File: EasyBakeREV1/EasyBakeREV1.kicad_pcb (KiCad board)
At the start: 2 copper layers, 100 x 71.2 mm, 135 parts, among them Q1 MMBT2222A, Q2 MMBT2222A, Q3 MMBT2222A, Q4 MMBT2222A, U1 MIC5219-3.3YM5, U10 STP08CP05, U11 MIC5219-5.0YM5, U12 NLSV2T244MU, U2 USBLC6-2SC6, U3 PCA9702, U4 SQ2310ES_SOT23, U5 NHD-C12832A1Z, U6 SQ2310ES_SOT23, U7 MAX31855_SO8, U8 LM324, U9 SN74LVC1G32, Y1 12MHz

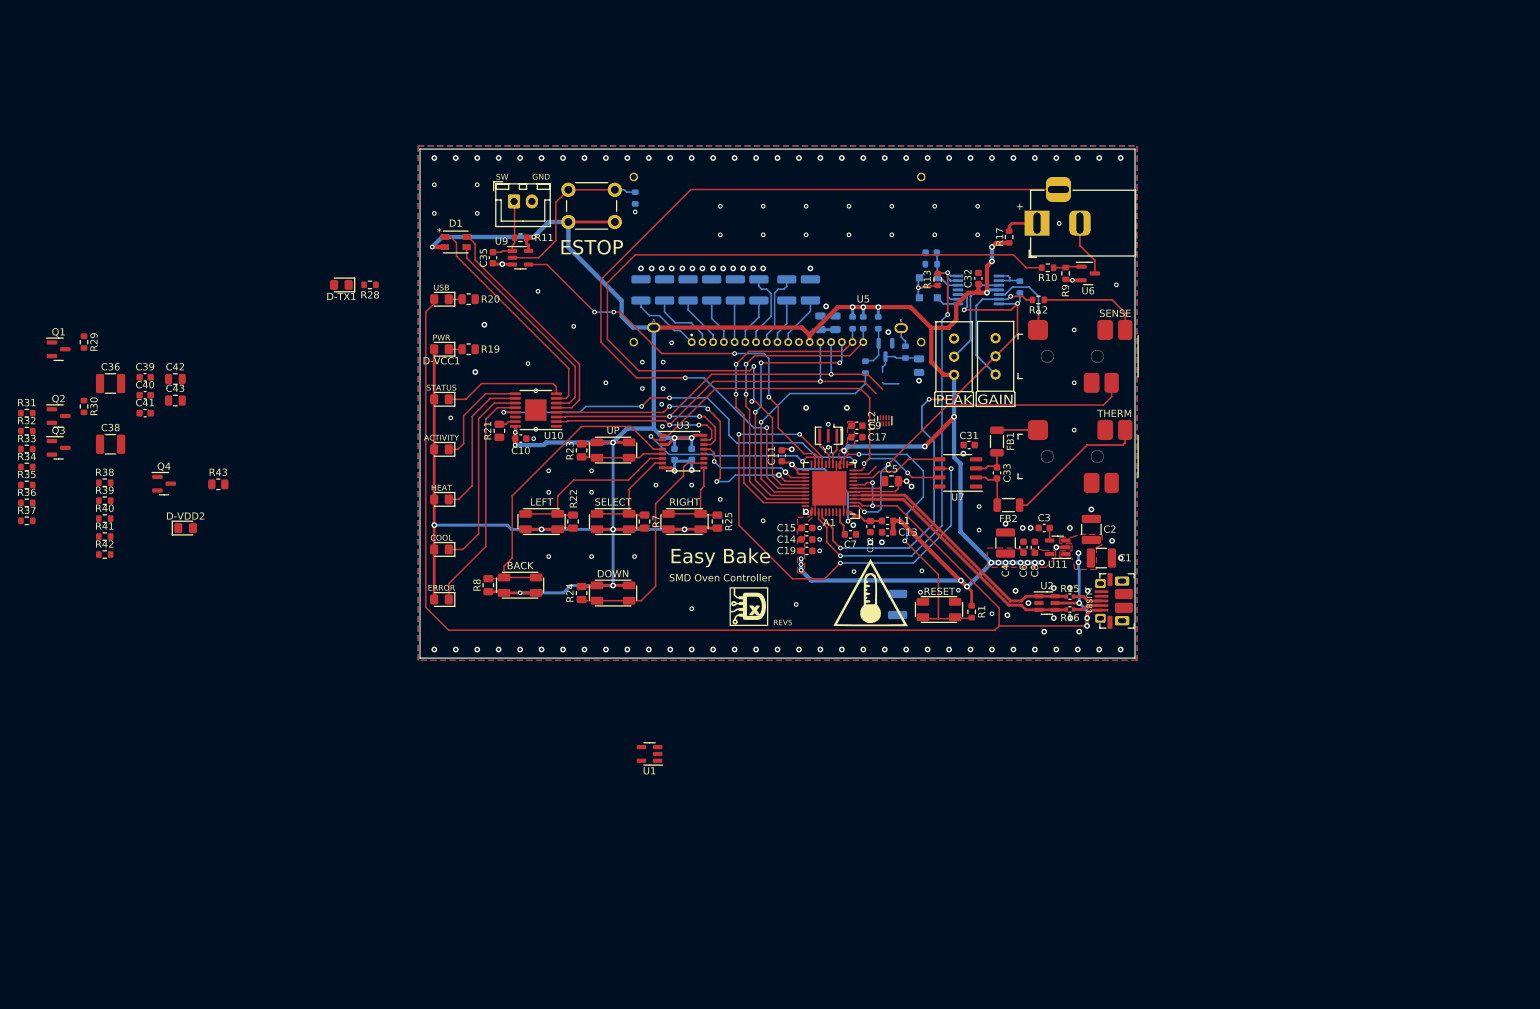
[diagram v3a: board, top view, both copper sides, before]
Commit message: Replaced MCU - started layout
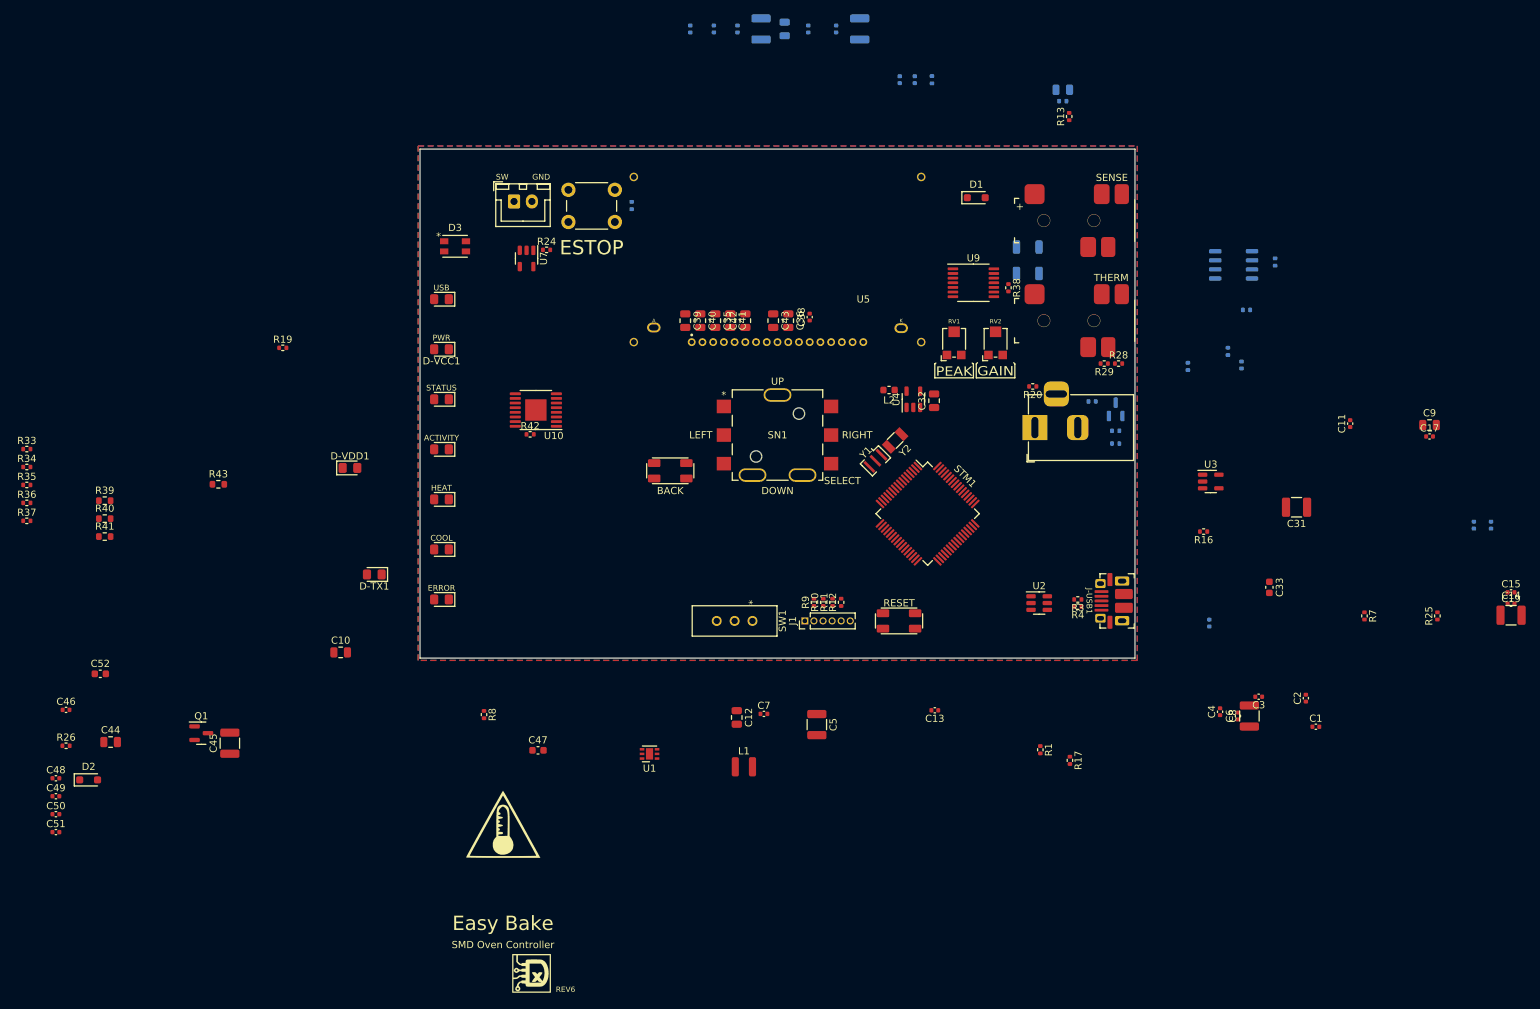
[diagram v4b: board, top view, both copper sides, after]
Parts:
- removed A1: PRO-MICRO-IC, Daxxn_Packages:QFN-44-1EP_7x7mm_P0.5mm_EP4.8x4.8mm
- removed D-VDD2: YELLOW, LED_SMD:LED_0805_2012Metric_Pad1.15x1.40mm_HandSolder
- removed D5, D6: General, Diode_SMD:D_SOD-323_HandSoldering
- removed Q2, Q3, Q4: MMBT2222A, Package_TO_SOT_SMD:SOT-23
- removed R30, R31: 10K, Resistor_SMD:R_0603_1608Metric
- removed R32: 1K, Resistor_SMD:R_0603_1608Metric
- removed SW-M-DN1, SW-M-L1, SW-M-R1, SW-M-UP1: SW_SPST, Daxxn_Switches:TL3365AF180QG
- removed SW-M-SEL1: TL3365, Daxxn_Switches:TL3365AF180QG
- removed U11: MIC5219-5.0YM5, Package_TO_SOT_SMD:SOT-23-5
- removed U12: NLSV2T244MU, Package_DFN_QFN:OnSemi_UDFN-8_1.2x1.8mm_P0.4mm
- added C44: 1uF, Capacitor_SMD:C_0805_2012Metric, F.Cu at (-28.3, 102.9)
- added C45: 10uF, Capacitor_SMD:C_1210_3225Metric, F.Cu at (-11.6, 103.1)
- added C46: 100nF, Capacitor_SMD:C_0402_1005Metric, F.Cu at (-34.5, 98.4)
- added C47: 100nF, Capacitor_SMD:C_0603_1608Metric, F.Cu at (31.5, 104.1)
- added C48: 100nF, Capacitor_SMD:C_0402_1005Metric, F.Cu at (-35.9, 108.0)
- added C49: 10nF, Capacitor_SMD:C_0402_1005Metric, F.Cu at (-35.9, 110.5)
- added C50: 100nF, Capacitor_SMD:C_0402_1005Metric, F.Cu at (-35.9, 113.0)
- added C51: 100nF, Capacitor_SMD:C_0402_1005Metric, F.Cu at (-35.9, 115.5)
- added C52: 100nF, Capacitor_SMD:C_0603_1608Metric, F.Cu at (-29.7, 93.4)
- added D-VDD1: YELLOW, LED_SMD:LED_0805_2012Metric_Pad1.15x1.40mm_HandSolder, F.Cu at (5.20, 64.6)
- added D2: General, Diode_SMD:D_SOD-323_HandSoldering, F.Cu at (-31.4, 108.2)
- added D3: LED_RGBA, Daxxn_LEDs:IN-P32TATRGB, F.Cu at (19.9, 33.6)
- added J1: SWD, Connector_PinHeader_1.27mm:PinHeader_1x06_P1.27mm_Vertical, F.Cu at (68.8, 86.0)
- added L2: 100nH, Inductor_SMD:L_0603_1608Metric, F.Cu at (80.6, 53.7)
- added R26: 22, Resistor_SMD:R_0402_1005Metric, F.Cu at (-34.5, 103.5)
- added SN1: JS5208, Daxxn_Switches:JS5208, F.Cu at (65.0, 60.0)
- added STM1: STM32F303RCT6TR, Package_QFP:LQFP-64_10x10mm_P0.5mm, F.Cu at (86.0, 71.0)
- added SW1: BOOT, Daxxn_Switches:EG1218, F.Cu at (61.5, 86.0)
- added Y2: 32.7KHz, Crystal:Crystal_SMD_3215-2Pin_3.2x1.5mm, F.Cu at (81.5, 60.8)
- C1, C38: value 10uF -> 100nF; footprint Capacitor_SMD:C_1210_3225Metric -> Capacitor_SMD:C_0402_1005Metric
- C10, C32, C34, C35, C39, C40, C9: value 100nF -> 1uF; footprint Capacitor_SMD:C_0603_1608Metric -> Capacitor_SMD:C_0805_2012Metric
- C11: value 100nF -> 10nF; footprint Capacitor_SMD:C_0603_1608Metric -> Capacitor_SMD:C_0402_1005Metric
- C12: value 100nF -> 4.7uF; footprint Capacitor_SMD:C_0603_1608Metric -> Capacitor_SMD:C_0805_2012Metric
- C13, C14, C15, C16, C17, C18, C6, C7: footprint Capacitor_SMD:C_0603_1608Metric -> Capacitor_SMD:C_0402_1005Metric
- C19, C31, C8: value 100nF -> 10uF; footprint Capacitor_SMD:C_0603_1608Metric -> Capacitor_SMD:C_1210_3225Metric
- C2: value 1uF -> 15pF; footprint Capacitor_SMD:C_1210_3225Metric -> Capacitor_SMD:C_0402_1005Metric
- C20, C21, C22, C29, C30, C37: value 1uF -> 100nF; footprint Capacitor_SMD:C_1210_3225Metric -> Capacitor_SMD:C_0402_1005Metric
- C23, C26: value 1uF -> 10uF
- C24: footprint Capacitor_SMD:C_1210_3225Metric -> Capacitor_SMD:C_0805_2012Metric
- C25: value 10uF -> 470pF; footprint Capacitor_SMD:C_0805_2012Metric -> Capacitor_SMD:C_0402_1005Metric
- C27, C28: footprint Capacitor_SMD:C_0805_2012Metric -> Capacitor_SMD:C_0402_1005Metric
- C3: value 470pF -> 15pF; footprint Capacitor_SMD:C_0603_1608Metric -> Capacitor_SMD:C_0402_1005Metric
- C33: value 10nF -> 470pF
- C36: value 10uF -> 1uF; footprint Capacitor_SMD:C_1210_3225Metric -> Capacitor_SMD:C_0805_2012Metric
- C4: value 10uF -> 22pF; footprint Capacitor_SMD:C_1210_3225Metric -> Capacitor_SMD:C_0402_1005Metric
- C41: value 470pF -> 1uF; footprint Capacitor_SMD:C_0603_1608Metric -> Capacitor_SMD:C_0805_2012Metric
- C42, C43: value 100nF -> 1uF
- C5: value 1uF -> 10uF; footprint Capacitor_SMD:C_0805_2012Metric -> Capacitor_SMD:C_1210_3225Metric
- D1: value LED_RGBA -> General; footprint Daxxn_LEDs:IN-P32TATRGB -> Diode_SMD:D_SOD-323_HandSoldering
- FB1, FB2, U6: moved to B.Cu
- L1: value 100nH -> 2.2uF; footprint Inductor_SMD:L_0603_1608Metric -> Daxxn_Passives:LQH3NPN
- Q1: value MMBT2222A -> SQ2310ES_SOT23
- R1, R13, R14, R18, R2, R27, R36, R38: footprint Resistor_SMD:R_0603_1608Metric -> Resistor_SMD:R_0402_1005Metric
- R10: value 100 -> 22; footprint Resistor_SMD:R_0603_1608Metric -> Resistor_SMD:R_0402_1005Metric
- R11, R9: value 10K -> 22; footprint Resistor_SMD:R_0603_1608Metric -> Resistor_SMD:R_0402_1005Metric
- R12: value 1K -> 22; footprint Resistor_SMD:R_0603_1608Metric -> Resistor_SMD:R_0402_1005Metric
- R15: value 22 -> 100; moved to B.Cu
- R16: value 22 -> 10K
- R17: value 100 -> 1K; footprint Resistor_SMD:R_0603_1608Metric -> Resistor_SMD:R_0402_1005Metric
- R19: value 1K -> 10K; footprint Resistor_SMD:R_0805_2012Metric -> Resistor_SMD:R_0402_1005Metric
- R20: value 1K -> 100; footprint Resistor_SMD:R_0805_2012Metric -> Resistor_SMD:R_0402_1005Metric
- R21: value 2K -> 100; footprint Resistor_SMD:R_0805_2012Metric -> Resistor_SMD:R_0402_1005Metric; moved to B.Cu
- R22: value 10K -> 100; footprint Resistor_SMD:R_0805_2012Metric -> Resistor_SMD:R_0402_1005Metric; moved to B.Cu
- R23: footprint Resistor_SMD:R_0805_2012Metric -> Resistor_SMD:R_0402_1005Metric; moved to B.Cu
- R24: footprint Resistor_SMD:R_0805_2012Metric -> Resistor_SMD:R_0402_1005Metric
- R25: value 10K -> 22; footprint Resistor_SMD:R_0805_2012Metric -> Resistor_SMD:R_0402_1005Metric
- R28: value 330 -> 10K; footprint Resistor_SMD:R_0603_1608Metric -> Resistor_SMD:R_0402_1005Metric
- R29, R35: value 10K -> 100; footprint Resistor_SMD:R_0603_1608Metric -> Resistor_SMD:R_0402_1005Metric
- R3, R4: value 10K -> 22; footprint Resistor_SMD:R_0603_1608Metric -> Resistor_SMD:R_0402_1005Metric; moved to F.Cu
- R33: value 1K -> 10K; footprint Resistor_SMD:R_0603_1608Metric -> Resistor_SMD:R_0402_1005Metric
- R34: value 1K -> 100; footprint Resistor_SMD:R_0603_1608Metric -> Resistor_SMD:R_0402_1005Metric
- R37: value 10K -> 1K; footprint Resistor_SMD:R_0603_1608Metric -> Resistor_SMD:R_0402_1005Metric
- R39: value 1K -> 330
- R40: value 10K -> 1K
- R41: value 100 -> 1K
- R42: value 100 -> 2K; footprint Resistor_SMD:R_0603_1608Metric -> Resistor_SMD:R_0402_1005Metric
- R43: footprint Resistor_SMD:R_0805_2012Metric -> Resistor_SMD:R_0603_1608Metric
- R5, R6: value 100 -> 10K; footprint Resistor_SMD:R_0603_1608Metric -> Resistor_SMD:R_0402_1005Metric
- R7: value 10K -> 430K; footprint Resistor_SMD:R_0805_2012Metric -> Resistor_SMD:R_0402_1005Metric
- R8: value 10K -> 100K; footprint Resistor_SMD:R_0805_2012Metric -> Resistor_SMD:R_0402_1005Metric
- RV1, RV2: footprint Potentiometer_THT:Potentiometer_Bourns_3296W_Vertical -> Daxxn_Switches:Bourns_TC33X
- U1: value MIC5219-3.3YM5 -> AP3401; footprint Package_TO_SOT_SMD:SOT-23-5 -> Package_DFN_QFN:DFN-6-1EP_2x2mm_P0.65mm_EP1x1.6mm
- U3: value PCA9702 -> MIC5219-5.0YM5; footprint Package_SO:SSOP-16_4.4x5.2mm_P0.65mm -> Package_TO_SOT_SMD:SOT-23-5
- U4: value SQ2310ES_SOT23 -> MIC5219-3.3YM5; footprint Package_TO_SOT_SMD:SOT-23 -> Package_TO_SOT_SMD:SOT-23-5; moved to F.Cu
- U7: value MAX31855_SO8 -> SN74LVC1G32; footprint Package_SO:SO-8_3.9x4.9mm_P1.27mm -> Package_TO_SOT_SMD:SOT-23-5
- U8: value LM324 -> MAX31855_SO8; footprint Package_SO:TSSOP-14_4.4x5mm_P0.65mm -> Package_SO:SO-8_3.9x4.9mm_P1.27mm
- U9: value SN74LVC1G32 -> LM324; footprint Package_TO_SOT_SMD:SOT-23-5 -> Package_SO:TSSOP-14_4.4x5mm_P0.65mm
- Y1: value 12MHz -> 16MHz; footprint Crystal:Resonator_SMD_Murata_CSTxExxV-3Pin_3.0x1.1mm -> Daxxn_Passives:Resonator_SMD_3Pin_3.0x1.1mm
- moved R29 142.7 mm to (110.7, 50.0), turned to 180 degrees
- moved R38 129.3 mm to (97.3, 39.4), turned to -90 degrees
- moved C16 112.2 mm to (164.8, 72.6)
- moved C18 112.2 mm to (162.4, 72.6)
- moved R28 105.3 mm to (112.7, 50.0), turned to 0 degrees
- moved R25 101.6 mm to (157.3, 85.3)
- moved R7 101.6 mm to (147.1, 85.3)
- moved C38 99.4 mm to (69.5, 43.5), turned to 90 degrees
- moved C14 98.9 mm to (167.6, 83.6)
- moved C15 98.9 mm to (167.6, 82.0)
- moved C19 98.9 mm to (167.6, 85.2)
- moved C36 95.2 mm to (66.5, 44.0), turned to -90 degrees
- moved C43 84.4 mm to (64.4, 44.0), turned to -90 degrees
- moved R21 83.0 mm to (109.0, 55.3), turned to 180 degrees
- moved C41 82.9 mm to (58.4, 44.0), turned to -90 degrees
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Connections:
- C1 pad 1: VBUS -> RESET
- C10 pad 1: VCC -> VDDA
- C11 pad 1: AVCC -> VDDA
- C12 pad 1: AVCC -> VDD
- C13 pad 1: VCC -> VDD
- C14 pad 1: VCC -> VDD
- C15 pad 1: VCC -> VDD
- C16 pad 1: VCC -> VDD
- C17 pad 1: VCC -> VDD
- C18 pad 1: VCC -> VDD
- C2 pad 1: VBUS -> Net-(STM1C-PC14)
- C20 pad 1: GND -> VCC
- C20 pad 2: Net-(U5-V_{0}) -> GND
- C21 pad 1: GND -> VCC
- C21 pad 2: Net-(U5-V_{1}) -> GND
- C22 pad 1: GND -> VCC
- C22 pad 2: Net-(U5-V_{2}) -> GND
- C23 pad 1: GND -> VBUS
- C23 pad 2: Net-(U5-V_{3}) -> GND
- C24 pad 1: GND -> VBUS
- C24 pad 2: Net-(U5-V_{4}) -> GND
- C25 pad 1: GND -> Net-(U3-BP)
- C25 pad 2: Net-(U4-D) -> GND
- C26 pad 1: GND -> Net-(U4-OUT)
- C26 pad 2: Net-(U5-V_{OUT}) -> GND
- C27 pad 1: VDD -> Net-(U4-OUT)
- C28 pad 1: VDD -> Net-(U4-OUT)
- C29 pad 1: Net-(U5-C2-) -> Net-(U4-OUT)
- C29 pad 2: Net-(U5-C2+) -> GND
- C3 pad 1: Net-(U1-BP) -> GND
- C3 pad 2: GND -> Net-(STM1C-PC15)
- C30 pad 1: Net-(U5-C1+) -> VDDA
- C30 pad 2: Net-(U5-C1-) -> GND
- C31 pad 1: VDD -> VCC
- C33 pad 1: Net-(U7-T+) -> Net-(U4-BP)
- C33 pad 2: Net-(U7-T-) -> GND
- C34 pad 1: Net-(D6-K) -> GND
- C34 pad 2: GND -> Net-(U5-V_{1})
- C35 pad 1: Net-(J-ESTOP1-Pin_1) -> GND
- C35 pad 2: GND -> Net-(U5-V_{3})
- C36 pad 1: VBUS -> GND
- C36 pad 2: GND -> Net-(U5-V_{OUT})
- C37 pad 1: VBUS -> VDD
- C38 pad 1: VCC -> VDD
- C39 pad 1: VCC -> GND
- C39 pad 2: GND -> Net-(U5-V_{0})
- C4 pad 2: GND -> Net-(U1-FB)
- C40 pad 1: VCC -> GND
- C40 pad 2: GND -> Net-(U5-V_{2})
- C41 pad 1: Net-(U11-BP) -> GND
- C41 pad 2: GND -> Net-(U5-V_{4})
- C42 pad 1: VCC -> Net-(U5-C2-)
- C42 pad 2: GND -> Net-(U5-C2+)
- C43 pad 1: VDD -> Net-(U5-C1+)
- C43 pad 2: GND -> Net-(U5-C1-)
- C5 pad 1: Net-(A1-UCAP) -> VDD
- C7 pad 1: Net-(A1-AREF) -> VDD
- C8 pad 1: VDD -> VBUS
- C9 pad 1: VCC -> VBUS
- D1 pad 1: /Indicators/IND-RED -> Net-(D1-K)
- D1 pad 2: VCC -> Net-(D1-A)
- FB1 pad 1: Net-(U7-T+) -> Net-(U8-T+)
- FB2 pad 1: Net-(U7-T-) -> Net-(U8-T-)
- J-ESTOP1 pad 2: GND -> Net-(J-ESTOP1-Pin_2)
- J-HTR1 pad 2: Net-(U6-D) -> Net-(J-HTR1-Pad2)
- J-HTR1 pad 3: /HTR-SW -> Net-(J-HTR1-Pad3)
- J-SENSE1 pad T: Net-(U8B-+) -> Net-(U9B-+)
- J-THERM1 pad SW: GND -> Net-(J-THERM1-PadSW)
- J-USB1 pad 6: GND -> unconnected-(J-USB1-Shield-Pad6)
- L1 pad 1: AVCC -> Net-(U1-LX)
- L1 pad 2: VCC -> VDD
- Q1 pad 1: GND -> Net-(Q1-G)
- Q1 pad 2: Net-(Q1-B) -> GND
- Q1 pad 3: /Display/DISP-A0-B -> Net-(Q1-D)
- R1 pad 1: unconnected-(R1-Pad1) -> Net-(STM1B-BOOT0)
- R1 pad 2: RESET -> Net-(SW1-B)
- R10 pad 1: /HTR-PWM -> Net-(J1-Pin_3)
- R10 pad 2: Net-(U6-G) -> /SWCLK
- R11 pad 1: Net-(J-ESTOP1-Pin_1) -> Net-(J1-Pin_4)
- R11 pad 2: VCC -> /SWDIO
- R12 pad 1: Net-(J-SENSE1-PadS) -> Net-(J1-Pin_5)
- R12 pad 2: Net-(U8B--) -> /SWO
- R13 pad 1: Net-(D5-K) -> VDD
- R13 pad 2: /CURR-PEAK -> /DISP-~{RESET}
- R14 pad 1: GND -> VDD
- R14 pad 2: Net-(D6-K) -> /DISP-~{CS}
- R15 pad 1: Net-(J-USB1-D+) -> Net-(U5-LED-)
- R15 pad 2: /USBIN+ -> Net-(Q1-D)
- R16 pad 1: Net-(J-USB1-D-) -> VDD
- R16 pad 2: /USBIN- -> Net-(Q1-G)
- R17 pad 1: Net-(J-HTR1-Pad1) -> Net-(Q1-G)
- R17 pad 2: VCC -> /DISP-BK-PWM
- R18 pad 1: /CURR-SENSE -> Net-(J-HTR1-Pad1)
- R18 pad 2: Net-(U8A--) -> VCC
- R19 pad 1: Net-(D-VCC1-K) -> /HTR-SW
- R19 pad 2: GND -> VCC
- R2 pad 2: /Display/DISP-~{RESET}-B -> RESET
- R20 pad 1: Net-(D-USB1-K) -> Net-(J-HTR1-Pad3)
- R20 pad 2: GND -> /HTR-SW
- R21 pad 1: Net-(U10-R-EXT) -> Net-(U6-D)
- R21 pad 2: GND -> Net-(J-HTR1-Pad2)
- R22 pad 1: /User_Control/MENU-LEFT -> /HTR-PWM
- R22 pad 2: VCC -> Net-(U6-G)
- R23 pad 1: /User_Control/MENU-UP -> Net-(U6-G)
- R23 pad 2: VCC -> GND
- R24 pad 1: VCC -> Net-(C47-Pad1)
- R24 pad 2: /User_Control/MENU-DOWN -> VCC
- R25 pad 1: VCC -> Net-(C47-Pad1)
- R25 pad 2: /User_Control/MENU-RIGHT -> Net-(J-ESTOP1-Pin_1)
- R28 pad 1: /TX-IND -> Net-(J-THERM1-PadSW)
- R28 pad 2: Net-(D-TX1-K) -> VCC
- R29 pad 1: VDD -> Net-(J-THERM1-PadSW)
- R29 pad 2: /Display/DISP-A0-B -> /THERM-SW
- R3 pad 1: VDD -> Net-(J-USB1-D+)
- R3 pad 2: /Display/DISP-~{CS}-B -> /USBIN+
- R33 pad 1: /DISP-RESET -> /CURR-SENSE-SW
- R33 pad 2: Net-(Q2-B) -> VCC
- R34 pad 1: Net-(Q3-B) -> /CURR-SENSE
- R34 pad 2: /DISP-CS -> /CURR-BIAS
- R35 pad 1: VDD -> /CURR-SENSE-SW
- R35 pad 2: Net-(Q2-B) -> Net-(J-SENSE1-PadSW)
- R36 pad 1: Net-(Q1-B) -> Net-(D1-K)
- R36 pad 2: GND -> /CURR-PEAK
- R37 pad 1: Net-(Q3-B) -> Net-(J-SENSE1-PadS)
- R37 pad 2: GND -> Net-(U9B--)
- R38 pad 1: VDD -> GND
- R38 pad 2: /Sensing/THERM-~{CS}-B -> Net-(D2-K)
- R39 pad 1: Net-(Q4-B) -> Net-(D-VDD1-K)
- R39 pad 2: /THERM-CS -> GND
- R4 pad 1: VCC -> Net-(J-USB1-D-)
- R4 pad 2: Net-(U4-G) -> /USBIN-
- R40 pad 1: Net-(Q4-B) -> Net-(D-VCC1-K)
- R41 pad 1: /CURR-SENSE-SW -> Net-(D-USB1-K)
- R41 pad 2: Net-(J-SENSE1-PadSW) -> GND
- R42 pad 1: /CURR-SENSE-SW -> Net-(U10-R-EXT)
- R42 pad 2: VCC -> GND
- R43 pad 1: Net-(D-VDD2-K) -> /TX-IND
- R43 pad 2: GND -> Net-(D-TX1-K)
- R5 pad 1: Net-(U4-G) -> VBUS
- R5 pad 2: /DISP-BK-PWM -> /MAIN-PG
- R6 pad 1: Net-(U5-LED-) -> VBUS
- R6 pad 2: Net-(U4-D) -> Net-(U1-EN)
- R7 pad 1: /User_Control/MENU-SELECT -> VDD
- R7 pad 2: VCC -> Net-(U1-FB)
- R8 pad 1: /User_Control/MENU-BACK -> Net-(U1-FB)
- R8 pad 2: VCC -> GND
- R9 pad 1: Net-(U6-G) -> Net-(J1-Pin_2)
- R9 pad 2: GND -> RESET
- RV1 pad 2: Net-(U8A-+) -> Net-(U9A-+)
- RV2 pad 3: Net-(U8B--) -> Net-(U9B--)
- SW-M-BK1 pad 1: /User_Control/MENU-BACK -> /MENU-BACK
- SW-M-BK1 pad 2: VCC -> GND
- U1 pad 1: VBUS -> Net-(U1-EN)
- U1 pad 2: GND -> /MAIN-PG
- U1 pad 4: Net-(U1-BP) -> Net-(U1-LX)
- U1 pad 5: VDD -> GND
- U10 pad 16: VCC -> VDD
- U3 pad 1: SPI-CIPO -> VBUS
- U3 pad 2: /IO-INT -> GND
- U3 pad 3: VDD -> VBUS
- U3 pad 4: /User_Control/MENU-BACK -> Net-(U3-BP)
- U3 pad 5: /User_Control/MENU-UP -> VCC
- U4 pad 1: Net-(U4-G) -> VCC
- U4 pad 3: Net-(U4-D) -> VCC
- U5 pad 13: SPI-COPI -> DISP-SPI-COPI
- U5 pad 14: SPI-SCLK -> DISP-SPI-SCLK
- U5 pad 15: /Display/DISP-A0-B -> /DISP-A0
- U5 pad 16: /Display/DISP-~{RESET}-B -> /DISP-~{RESET}
- U5 pad 17: /Display/DISP-~{CS}-B -> /DISP-~{CS}
- U7 pad 1: GND -> Net-(C47-Pad1)
- U7 pad 2: Net-(U7-T-) -> Net-(SW-ESTOP1-A)
- U7 pad 3: Net-(U7-T+) -> GND
- U7 pad 4: VDD -> /ESTOP-SW
- U7 pad 5: SPI-SCLK -> VCC
- U8 pad 1: Net-(U8A--) -> GND
- U8 pad 2: Net-(U8A--) -> Net-(U8-T-)
- U8 pad 3: Net-(U8A-+) -> Net-(U8-T+)
- U8 pad 4: VCC -> VDD
- U8 pad 5: Net-(U8B-+) -> SPI-SCLK
- U8 pad 6: Net-(U8B--) -> /THERM-~{CS}
- U8 pad 7: /CURR-SENSE -> SPI-CIPO
- U8 pad 8: Net-(D5-A) -> (no net)
- U9 pad 1: Net-(J-ESTOP1-Pin_1) -> /CURR-BIAS
- U9 pad 2: Net-(SW-ESTOP1-A) -> /CURR-BIAS
- U9 pad 3: GND -> Net-(U9A-+)
- U9 pad 4: /ESTOP-SW -> VCC
- U9 pad 5: VCC -> Net-(U9B-+)
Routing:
- net VCC: track 437.7 -> 0.00 mm, vias 35 -> 0
- net VBUS: track 190.8 -> 0.00 mm, vias 7 -> 0
- net /HTR-SW: track 119.1 -> 0.00 mm, vias 2 -> 0
- net /HTR-PWM: track 115.7 -> 0.00 mm, vias 2 -> 0
- net SPI-SCLK: track 77.2 -> 0.00 mm, vias 3 -> 0
- net /CURR-SENSE: track 75.0 -> 0.00 mm, vias 4 -> 0
- net /THERM-CS: track 72.2 -> 0.00 mm, vias 4 -> 0
- net /CURR-PEAK: track 64.4 -> 0.00 mm, vias 3 -> 0
- net SPI-COPI: track 62.3 -> 0.00 mm, vias 3 -> 0
- net /IND-OE: track 57.8 -> 0.00 mm, vias 4 -> 0
- net /ESTOP-SW: track 57.6 -> 0.00 mm, vias 4 -> 0
- net SPI-CIPO: track 55.9 -> 0.00 mm, vias 2 -> 0
- net /CURR-SENSE-SW: track 48.2 -> 0.00 mm, vias 2 -> 0
- net /DISP-RESET: track 46.3 -> 0.00 mm, vias 2 -> 0
- net /IND-LE: track 45.9 -> 0.00 mm, vias 4 -> 0
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- removed copper zone on F.Cu, net VBUS
- removed copper zone on F.Cu, net VCC
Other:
- board text added: "REV6"
- board text removed: "PWM BYPASS"
- board text removed: "REV5"

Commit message: Rearrange footprints and start layout
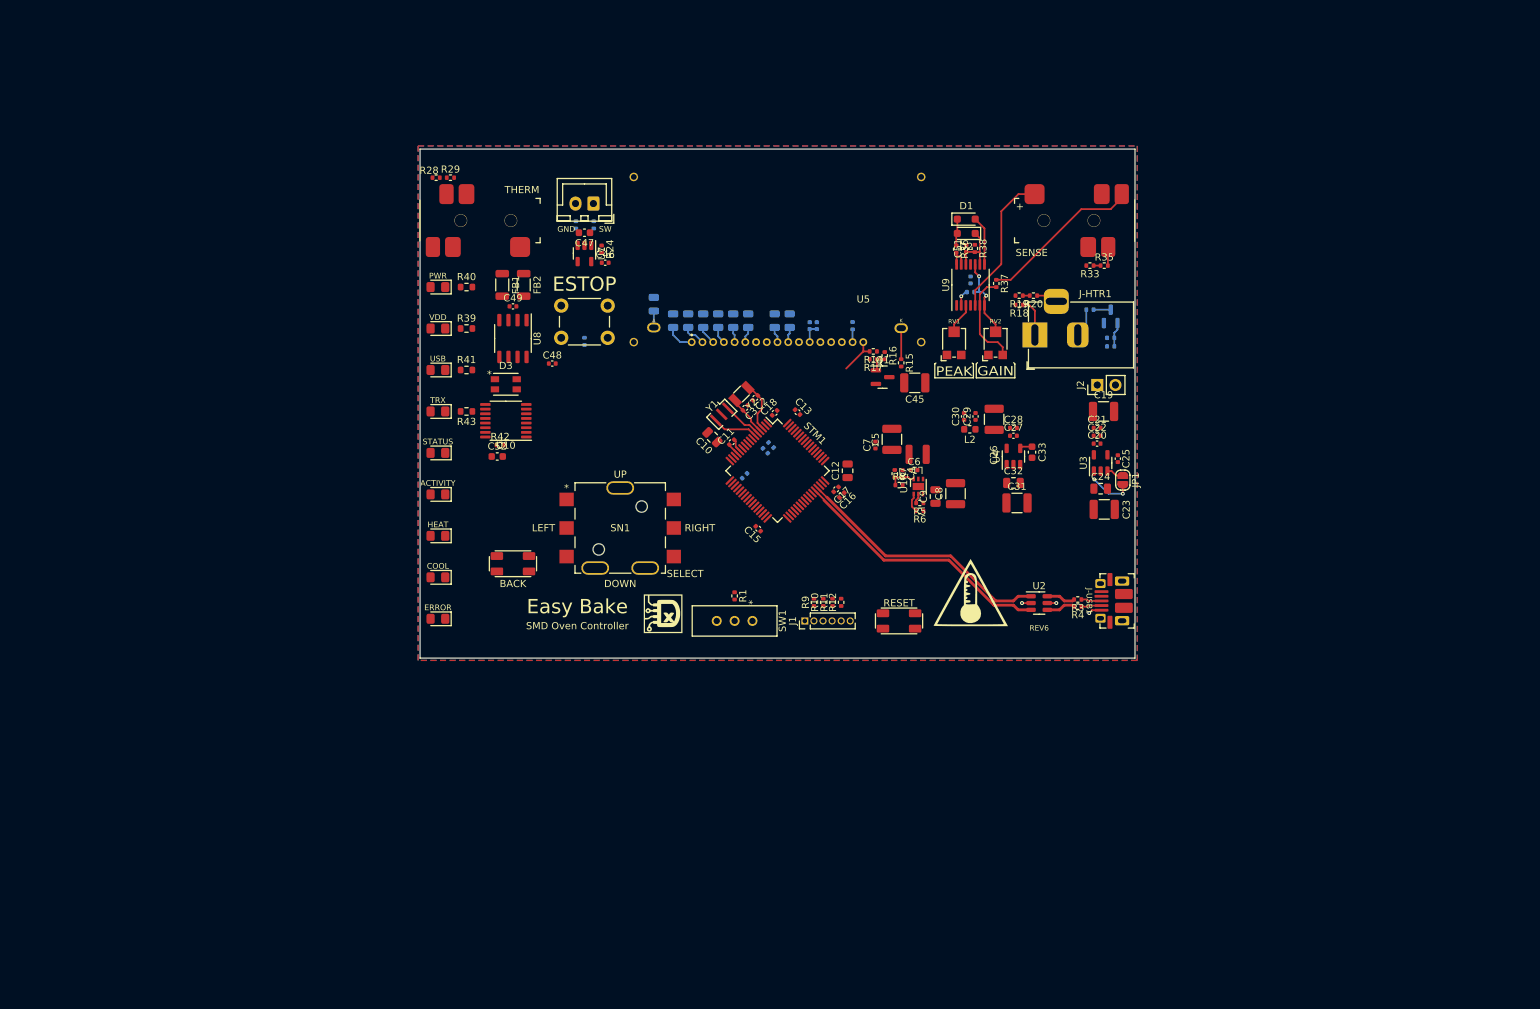
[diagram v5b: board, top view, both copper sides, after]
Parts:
- added J2: PWR, Connector_PinHeader_2.54mm:PinHeader_1x02_P2.54mm_Vertical, F.Cu at (109.7, 53.0)
- added JP1: USB-PWR-EN, Jumper:SolderJumper-2_P1.3mm_Open_RoundedPad1.0x1.5mm, F.Cu at (113.3, 66.3)
- C1, C14, C35, C36, C38, C39, C40, C41, C44, C50, R13, R25, R26, R34: moved to B.Cu
- C16, C18, C20, C21, C22, C23, C24, C25, C26, C27, C28, C29, C30, FB1, FB2, R14, R15, R18, R5, R6, U8: moved to F.Cu
- C42, C43: value 1uF -> 2.2uF; moved to B.Cu
- C47: value 100nF -> 1uF
- J-HTR1: footprint Connector_BarrelJack:BarrelJack_Horizontal -> Daxxn_Connectors:BarrelJack_Horizontal
- U10: footprint Package_SO:TSSOP-16-1EP_4.4x5mm_P0.65mm_EP3x3mm -> Package_SO:TSSOP-16_4.4x5mm_P0.65mm
- Y2: footprint Crystal:Crystal_SMD_3215-2Pin_3.2x1.5mm -> Daxxn_Passives:Crystal_SMD_3215-2Pin_3.2x1.5mm
- moved R35 153.8 mm to (110.7, 36.3)
- moved C51 151.3 mm to (91.4, 33.9), turned to 90 degrees
- moved R33 150.9 mm to (108.7, 36.3), turned to 180 degrees
- moved C50 148.2 mm to (92.0, 38.3), turned to 90 degrees
- moved D2 144.6 mm to (91.4, 31.8), turned to 180 degrees
- moved R37 139.6 mm to (95.6, 38.8), turned to -90 degrees
- moved R36 134.8 mm to (90.0, 34.0), turned to -90 degrees
- moved R34 134.2 mm to (92.0, 40.0), turned to 180 degrees
- moved R25 130.1 mm to (39.3, 30.6)
- moved C14 108.7 mm to (60.4, 65.7), turned to 45 degrees
- moved C45 108.2 mm to (84.2, 52.7), turned to 180 degrees
- moved Q1 107.5 mm to (79.7, 51.9)
- moved C15 105.7 mm to (62.3, 73.1), turned to 135 degrees
- moved R19 103.3 mm to (98.8, 40.5), turned to 180 degrees
- moved R26 101.9 mm to (36.8, 30.6), turned to -90 degrees
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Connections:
- J-THERM1 pad S: Net-(FB2-Pad2) -> Net-(FB1-Pad2)
- J-THERM1 pad T: Net-(FB1-Pad2) -> Net-(FB2-Pad2)
- U3 pad 3: VBUS -> Net-(JP1-A)
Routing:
- net /USBIN-: track 0.00 -> 41.3 mm
- net /USBIN+: track 0.00 -> 40.8 mm
- net Net-(J-SENSE1-PadS): track 0.00 -> 22.8 mm
- net Net-(U9B-+): track 0.00 -> 20.3 mm
- net Net-(U9B--): track 0.00 -> 13.4 mm
- net /CURR-SENSE: track 0.00 -> 11.8 mm, vias 0 -> 2
- net VBUS: track 0.00 -> 9.22 mm, vias 0 -> 4
- net Net-(D2-K): track 0.00 -> 8.30 mm
- net Net-(STM1C-PC14): track 0.00 -> 7.21 mm
- net Net-(D1-A): track 0.00 -> 6.88 mm
- net Net-(STM1B-OSC-OUT): track 0.00 -> 6.41 mm
- net Net-(STM1C-PC15): track 0.00 -> 5.70 mm
- net Net-(STM1B-OSC-IN): track 0.00 -> 5.63 mm
- net /DISP-~{CS}: track 0.00 -> 5.58 mm
- net Net-(J-HTR1-Pad1): track 0.00 -> 5.42 mm
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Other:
- board text added: "TRX"
- board text added: "VDD"
